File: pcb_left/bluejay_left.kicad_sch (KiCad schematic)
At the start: 72 parts, among them J1 SJ-43514, U1 ATmega328P-PU, Y1 16MHz

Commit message: Further work on pcbs
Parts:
- DZ1, DZ2: footprint Diode_THT_AKL:D_DO-35_SOD27_P7.62mm_Horizontal_Zener -> BlueJay footprints:D_DO-35_SOD27_P5.08mm_Horizontal
- Da1, Da2, Da3, Da4, Da5, Db1, Db2, Db3, Db4, Db5, Dc1, Dc2, Dc3, Dc4, Dc5, Dd1, Dd2, Dd3, Dd4, Dd5, De1, De2, De3, De4, Df2, Df3, Df4: footprint Diode_THT_AKL:D_DO-35_SOD27_P7.62mm_Horizontal -> BlueJay footprints:D_DO-35_SOD27_P5.08mm_Horizontal
- SWa1, SWa2, SWa3, SWa4, SWa5, SWb1, SWb2, SWb3, SWb4, SWb5, SWc1, SWc2, SWc3, SWc4, SWc5, SWd1, SWd2, SWd3, SWd4, SWd5, SWe1, SWe2, SWe3, SWe4, SWf2, SWf3, SWf4: footprint BlueJay footprints:Kailh_socket_MX -> Switch_Keyboard_Cherry_MX:SW_Cherry_MX_PCB_1.00u

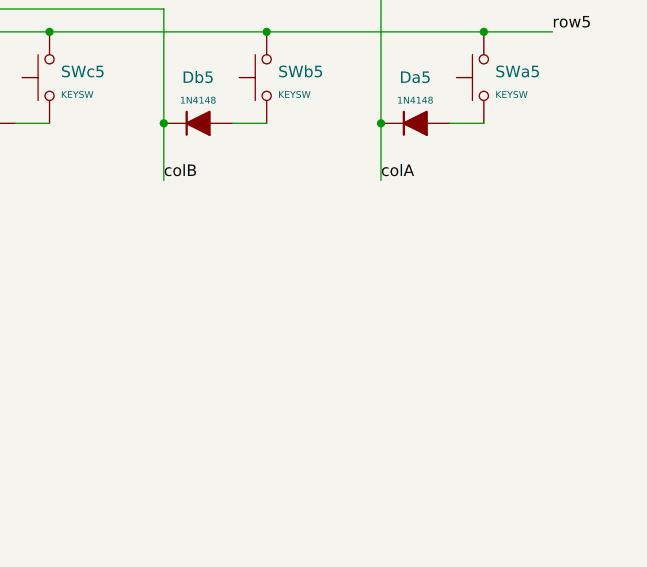
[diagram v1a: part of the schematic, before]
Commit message: Add mounting holes
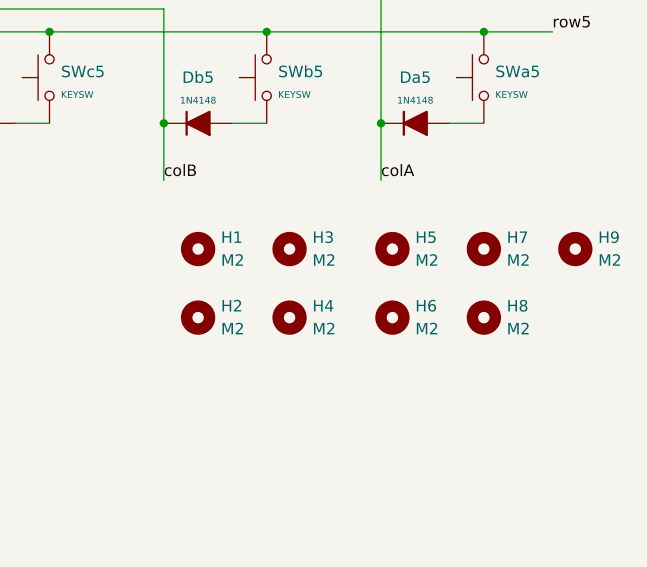
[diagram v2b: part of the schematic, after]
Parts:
- added H1, H2, H3, H4, H5, H6, H7, H8, H9: M2, MountingHole:MountingHole_2.2mm_M2_Pad, symbol Mechanical:MountingHole
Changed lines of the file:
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@@
     (pin "2")
+  )
+  (symbol (lib_id "Mechanical:MountingHole") (at 215.9 162.56 0) (unit 1)
+    (in_bom no) (on_board yes) (fields_autoplaced)
+    (property "Reference" "H2" (id 0) (at 218.44 161.2899 0)
+      (effects (font (size 1.27 1.27)) (justify left))
+    )
+    (property "Value" "M2" (id 1) (at 218.44 163.8299 0)
+      (effects (font (size 1.27 1.27)) (justify left))
+    )
+    (property "Footprint" "MountingHole:MountingHole_2.2mm_M2_Pad" (id 2) (at 215.9 162.56 0)
+      (effects (font (size 1.27 1.27)) hide)
+    )
+    (property "Datasheet" "~" (id 3) (at 215.9 162.56 0)
+      (effects (font (size 1.27 1.27)) hide)
+    )
   )
   (symbol (lib_id "power:GND") (at 93.98 193.04 0) (unit 1)
@@
     (pin "2")
   )
+  (symbol (lib_id "Mechanical:MountingHole") (at 226.06 154.94 0) (unit 1)
+    (in_bom no) (on_board yes) (fields_autoplaced)
+    (property "Reference" "H3" (id 0) (at 228.6 153.6699 0)
+      (effects (font (size 1.27 1.27)) (justify left))
+    )
+    (property "Value" "M2" (id 1) (at 228.6 156.2099 0)
+      (effects (font (size 1.27 1.27)) (justify left))
+    )
+    (property "Footprint" "MountingHole:MountingHole_2.2mm_M2_Pad" (id 2) (at 226.06 154.94 0)
+      (effects (font (size 1.27 1.27)) hide)
+    )
+    (property "Datasheet" "~" (id 3) (at 226.06 154.94 0)
+      (effects (font (size 1.27 1.27)) hide)
+    )
+  )
   (symbol (lib_id "power:PWR_FLAG") (at 29.21 92.71 90) (unit 1)
     (in_bom yes) (on_board yes)
@@
     (pin "1")
     (pin "2")
+  )
+  (symbol (lib_id "Mechanical:MountingHole") (at 237.49 162.56 0) (unit 1)
+    (in_bom no) (on_board yes) (fields_autoplaced)
+    (property "Reference" "H6" (id 0) (at 240.03 161.2899 0)
+      (effects (font (size 1.27 1.27)) (justify left))
+    )
+    (property "Value" "M2" (id 1) (at 240.03 163.8299 0)
+      (effects (font (size 1.27 1.27)) (justify left))
+    )
+    (property "Footprint" "MountingHole:MountingHole_2.2mm_M2_Pad" (id 2) (at 237.49 162.56 0)
+      (effects (font (size 1.27 1.27)) hide)
+    )
+    (property "Datasheet" "~" (id 3) (at 237.49 162.56 0)
+      (effects (font (size 1.27 1.27)) hide)
+    )
   )
   (symbol (lib_id "BlueJaySymbolLibrary:0548190519") (at 24.13 77.47 0) (unit 1)
@@
     (pin "SH")
   )
+  (symbol (lib_id "Mechanical:MountingHole") (at 237.49 154.94 0) (unit 1)
+    (in_bom no) (on_board yes) (fields_autoplaced)
+    (property "Reference" "H5" (id 0) (at 240.03 153.6699 0)
+      (effects (font (size 1.27 1.27)) (justify left))
+    )
+    (property "Value" "M2" (id 1) (at 240.03 156.2099 0)
+      (effects (font (size 1.27 1.27)) (justify left))
+    )
+    (property "Footprint" "MountingHole:MountingHole_2.2mm_M2_Pad" (id 2) (at 237.49 154.94 0)
+      (effects (font (size 1.27 1.27)) hide)
+    )
+    (property "Datasheet" "~" (id 3) (at 237.49 154.94 0)
+      (effects (font (size 1.27 1.27)) hide)
+    )
+  )
   (symbol (lib_id "BlueJaySymbolLibrary:C_Small") (at 59.69 137.16 90) (unit 1)
     (in_bom yes) (on_board yes) (fields_autoplaced)
@@
     (pin "1")
   )
+  (symbol (lib_id "Mechanical:MountingHole") (at 257.81 154.94 0) (unit 1)
+    (in_bom no) (on_board yes) (fields_autoplaced)
+    (property "Reference" "H9" (id 0) (at 260.35 153.6699 0)
+      (effects (font (size 1.27 1.27)) (justify left))
+    )
+    (property "Value" "M2" (id 1) (at 260.35 156.2099 0)
+      (effects (font (size 1.27 1.27)) (justify left))
+    )
+    (property "Footprint" "MountingHole:MountingHole_2.2mm_M2_Pad" (id 2) (at 257.81 154.94 0)
+      (effects (font (size 1.27 1.27)) hide)
+    )
+    (property "Datasheet" "~" (id 3) (at 257.81 154.94 0)
+      (effects (font (size 1.27 1.27)) hide)
+    )
+  )
   (symbol (lib_id "Diode_AKL:1N4148") (at 162.56 99.06 180) (unit 1)
     (in_bom yes) (on_board yes) (fields_autoplaced)
@@
     (pin "1")
     (pin "2")
+  )
+  (symbol (lib_id "Mechanical:MountingHole") (at 247.65 154.94 0) (unit 1)
+    (in_bom no) (on_board yes) (fields_autoplaced)
+    (property "Reference" "H7" (id 0) (at 250.19 153.6699 0)
+      (effects (font (size 1.27 1.27)) (justify left))
+    )
+    (property "Value" "M2" (id 1) (at 250.19 156.2099 0)
+      (effects (font (size 1.27 1.27)) (justify left))
+    )
+    (property "Footprint" "MountingHole:MountingHole_2.2mm_M2_Pad" (id 2) (at 247.65 154.94 0)
+      (effects (font (size 1.27 1.27)) hide)
+    )
+    (property "Datasheet" "~" (id 3) (at 247.65 154.94 0)
+      (effects (font (size 1.27 1.27)) hide)
+    )
   )
   (symbol (lib_id "Diode_AKL:1N4148") (at 138.43 99.06 180) (unit 1)
@@
     (pin "2")
   )
+  (symbol (lib_id "Mechanical:MountingHole") (at 247.65 162.56 0) (unit 1)
+    (in_bom no) (on_board yes) (fields_autoplaced)
+    (property "Reference" "H8" (id 0) (at 250.19 161.2899 0)
+      (effects (font (size 1.27 1.27)) (justify left))
+    )
+    (property "Value" "M2" (id 1) (at 250.19 163.8299 0)
+      (effects (font (size 1.27 1.27)) (justify left))
+    )
+    (property "Footprint" "MountingHole:MountingHole_2.2mm_M2_Pad" (id 2) (at 247.65 162.56 0)
+      (effects (font (size 1.27 1.27)) hide)
+    )
+    (property "Datasheet" "~" (id 3) (at 247.65 162.56 0)
+      (effects (font (size 1.27 1.27)) hide)
+    )
+  )
   (symbol (lib_id "BlueJaySymbolLibrary:Switch_SW_Push") (at 194.31 81.28 90) (unit 1)
     (in_bom yes) (on_board yes) (fields_autoplaced)
@@
     (pin "2")
   )
+  (symbol (lib_id "Mechanical:MountingHole") (at 226.06 162.56 0) (unit 1)
+    (in_bom no) (on_board yes) (fields_autoplaced)
+    (property "Reference" "H4" (id 0) (at 228.6 161.2899 0)
+      (effects (font (size 1.27 1.27)) (justify left))
+    )
+    (property "Value" "M2" (id 1) (at 228.6 163.8299 0)
+      (effects (font (size 1.27 1.27)) (justify left))
+    )
+    (property "Footprint" "MountingHole:MountingHole_2.2mm_M2_Pad" (id 2) (at 226.06 162.56 0)
+      (effects (font (size 1.27 1.27)) hide)
+    )
+    (property "Datasheet" "~" (id 3) (at 226.06 162.56 0)
+      (effects (font (size 1.27 1.27)) hide)
+    )
+  )
   (symbol (lib_id "BlueJaySymbolLibrary:Switch_SW_Push") (at 247.65 135.89 90) (unit 1)
     (in_bom yes) (on_board yes) (fields_autoplaced)
@@
     (pin "1")
     (pin "2")
+  )
+  (symbol (lib_id "Mechanical:MountingHole") (at 215.9 154.94 0) (unit 1)
+    (in_bom no) (on_board yes) (fields_autoplaced)
+    (property "Reference" "H1" (id 0) (at 218.44 153.6699 0)
+      (effects (font (size 1.27 1.27)) (justify left))
+    )
+    (property "Value" "M2" (id 1) (at 218.44 156.2099 0)
+      (effects (font (size 1.27 1.27)) (justify left))
+    )
+    (property "Footprint" "MountingHole:MountingHole_2.2mm_M2_Pad" (id 2) (at 215.9 154.94 0)
+      (effects (font (size 1.27 1.27)) hide)
+    )
+    (property "Datasheet" "~" (id 3) (at 215.9 154.94 0)
+      (effects (font (size 1.27 1.27)) hide)
+    )
   )
   (symbol (lib_id "Diode_AKL:1N4148") (at 90.17 111.76 180) (unit 1)
@@
       (reference "F1") (unit 1) (value "100mA") (footprint "BlueJay footprints:polyfuse_5.1mm")
     )
+    (path "/d0420dde-bff1-4dd4-b50e-a8ff439a9375"
+      (reference "H1") (unit 1) (value "M2") (footprint "MountingHole:MountingHole_2.2mm_M2_Pad")
+    )
+    (path "/4a35a674-388c-438a-8da0-ee33b6fc37e8"
+      (reference "H2") (unit 1) (value "M2") (footprint "MountingHole:MountingHole_2.2mm_M2_Pad")
+    )
+    (path "/552b5d1f-a593-40c3-a973-202071f3c188"
+      (reference "H3") (unit 1) (value "M2") (footprint "MountingHole:MountingHole_2.2mm_M2_Pad")
+    )
+    (path "/c9aec2e8-4e37-4baa-9790-b0363dbc3f18"
+      (reference "H4") (unit 1) (value "M2") (footprint "MountingHole:MountingHole_2.2mm_M2_Pad")
+    )
+    (path "/6dcbd964-e53a-42c2-bb2f-1604534332d7"
+      (reference "H5") (unit 1) (value "M2") (footprint "MountingHole:MountingHole_2.2mm_M2_Pad")
+    )
+    (path "/6133af06-e5a9-4dea-9d88-3fa37672e076"
+      (reference "H6") (unit 1) (value "M2") (footprint "MountingHole:MountingHole_2.2mm_M2_Pad")
+    )
+    (path "/8ff55002-cb98-4e23-b57e-209cc7ec712a"
+      (reference "H7") (unit 1) (value "M2") (footprint "MountingHole:MountingHole_2.2mm_M2_Pad")
+    )
+    (path "/a73aae4f-b04b-4d16-8b11-ca3d57da8772"
+      (reference "H8") (unit 1) (value "M2") (footprint "MountingHole:MountingHole_2.2mm_M2_Pad")
+    )
+    (path "/88babb1f-a86c-44c4-9ecd-f3e8d1f4aef4"
+      (reference "H9") (unit 1) (value "M2") (footprint "MountingHole:MountingHole_2.2mm_M2_Pad")
+    )
     (path "/36a90cbb-ec70-4202-aacd-9cf629bac560"

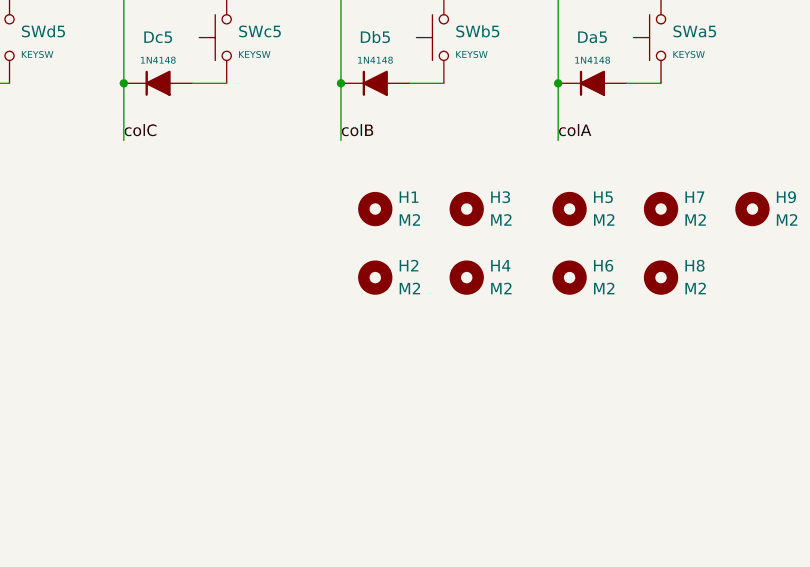
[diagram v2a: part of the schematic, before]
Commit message: Ground a couple mounting holes so as to ground plate and base too
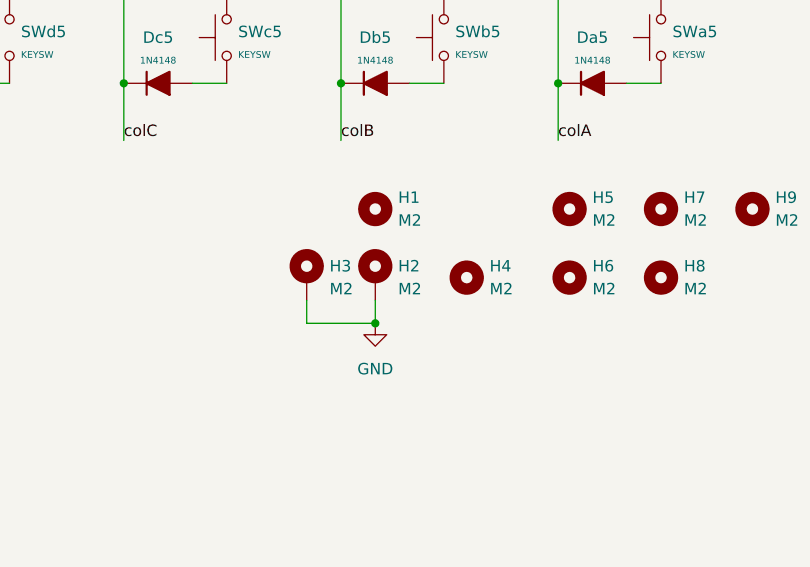
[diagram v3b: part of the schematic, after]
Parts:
- H2, H3: symbol Mechanical:MountingHole -> Mechanical:MountingHole_Pad; now in the parts list
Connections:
- net GND: now also H2.1, H3.1
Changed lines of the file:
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@@
   (junction (at 182.88 111.76) (diameter 0) (color 0 0 0 0)
+  )
+  (junction (at 215.9 167.64) (diameter 0) (color 0 0 0 0)
   )
   (junction (at 207.01 111.76) (diameter 0) (color 0 0 0 0)
@@
     (stroke (width 0) (type default) (color 0 0 0 0))
   )
+  (wire (pts (xy 208.28 167.64) (xy 215.9 167.64))
+    (stroke (width 0) (type default) (color 0 0 0 0))
+  )
   (wire (pts (xy 93.98 184.15) (xy 93.98 185.42))
     (stroke (width 0) (type default) (color 0 0 0 0))
@@
     (stroke (width 0) (type default) (color 0 0 0 0))
   )
+  (wire (pts (xy 208.28 165.1) (xy 208.28 167.64))
+    (stroke (width 0) (type default) (color 0 0 0 0))
+  )
   (wire (pts (xy 118.11 111.76) (xy 121.92 111.76))
     (stroke (width 0) (type default) (color 0 0 0 0))
@@
   )
   (wire (pts (xy 115.57 162.56) (xy 116.84 162.56))
+    (stroke (width 0) (type default) (color 0 0 0 0))
+  )
+  (wire (pts (xy 215.9 165.1) (xy 215.9 167.64))
     (stroke (width 0) (type default) (color 0 0 0 0))
   )
@@
     (pin "2")
   )
-  (symbol (lib_id "Mechanical:MountingHole") (at 215.9 162.56 0) (unit 1)
-    (in_bom no) (on_board yes) (fields_autoplaced)
+  (symbol (lib_id "Mechanical:MountingHole_Pad") (at 215.9 162.56 0) (unit 1)
+    (in_bom yes) (on_board yes) (fields_autoplaced)
     (property "Reference" "H2" (id 0) (at 218.44 161.2899 0)
       (effects (font (size 1.27 1.27)) (justify left))
@@
       (effects (font (size 1.27 1.27)) hide)
     )
+    (pin "1")
   )
   (symbol (lib_id "power:GND") (at 93.98 193.04 0) (unit 1)
@@
     (pin "2")
   )
-  (symbol (lib_id "Mechanical:MountingHole") (at 226.06 154.94 0) (unit 1)
-    (in_bom no) (on_board yes) (fields_autoplaced)
-    (property "Reference" "H3" (id 0) (at 228.6 153.6699 0)
-      (effects (font (size 1.27 1.27)) (justify left))
-    )
-    (property "Value" "M2" (id 1) (at 228.6 156.2099 0)
-      (effects (font (size 1.27 1.27)) (justify left))
-    )
-    (property "Footprint" "MountingHole:MountingHole_2.2mm_M2_Pad" (id 2) (at 226.06 154.94 0)
-      (effects (font (size 1.27 1.27)) hide)
-    )
-    (property "Datasheet" "~" (id 3) (at 226.06 154.94 0)
-      (effects (font (size 1.27 1.27)) hide)
-    )
+  (symbol (lib_id "Mechanical:MountingHole_Pad") (at 208.28 162.56 0) (unit 1)
+    (in_bom yes) (on_board yes) (fields_autoplaced)
+    (property "Reference" "H3" (id 0) (at 210.82 161.2899 0)
+      (effects (font (size 1.27 1.27)) (justify left))
+    )
+    (property "Value" "M2" (id 1) (at 210.82 163.8299 0)
+      (effects (font (size 1.27 1.27)) (justify left))
+    )
+    (property "Footprint" "MountingHole:MountingHole_2.2mm_M2_Pad" (id 2) (at 208.28 162.56 0)
+      (effects (font (size 1.27 1.27)) hide)
+    )
+    (property "Datasheet" "~" (id 3) (at 208.28 162.56 0)
+      (effects (font (size 1.27 1.27)) hide)
+    )
+    (pin "1")
   )
   (symbol (lib_id "power:PWR_FLAG") (at 29.21 92.71 90) (unit 1)
@@
     (pin "1")
     (pin "2")
+  )
+  (symbol (lib_id "power:GND") (at 215.9 167.64 0) (unit 1)
+    (in_bom yes) (on_board yes) (fields_autoplaced)
+    (property "Reference" "#PWR?" (id 0) (at 215.9 173.99 0)
+      (effects (font (size 1.27 1.27)) hide)
+    )
+    (property "Value" "GND" (id 1) (at 215.9 172.72 0))
+    (property "Footprint" "" (id 2) (at 215.9 167.64 0)
+      (effects (font (size 1.27 1.27)) hide)
+    )
+    (property "Datasheet" "" (id 3) (at 215.9 167.64 0)
+      (effects (font (size 1.27 1.27)) hide)
+    )
+    (pin "1")
   )
   (symbol (lib_id "power:VCC") (at 64.77 154.94 0) (unit 1)
@@
       (reference "#PWR0114") (unit 1) (value "GND") (footprint "")
     )
+    (path "/aa799aa4-0b77-4e69-bd3a-b95b04823f1a"
+      (reference "#PWR?") (unit 1) (value "GND") (footprint "")
+    )
     (path "/709a6874-5923-446e-9322-a60e23d13f71"

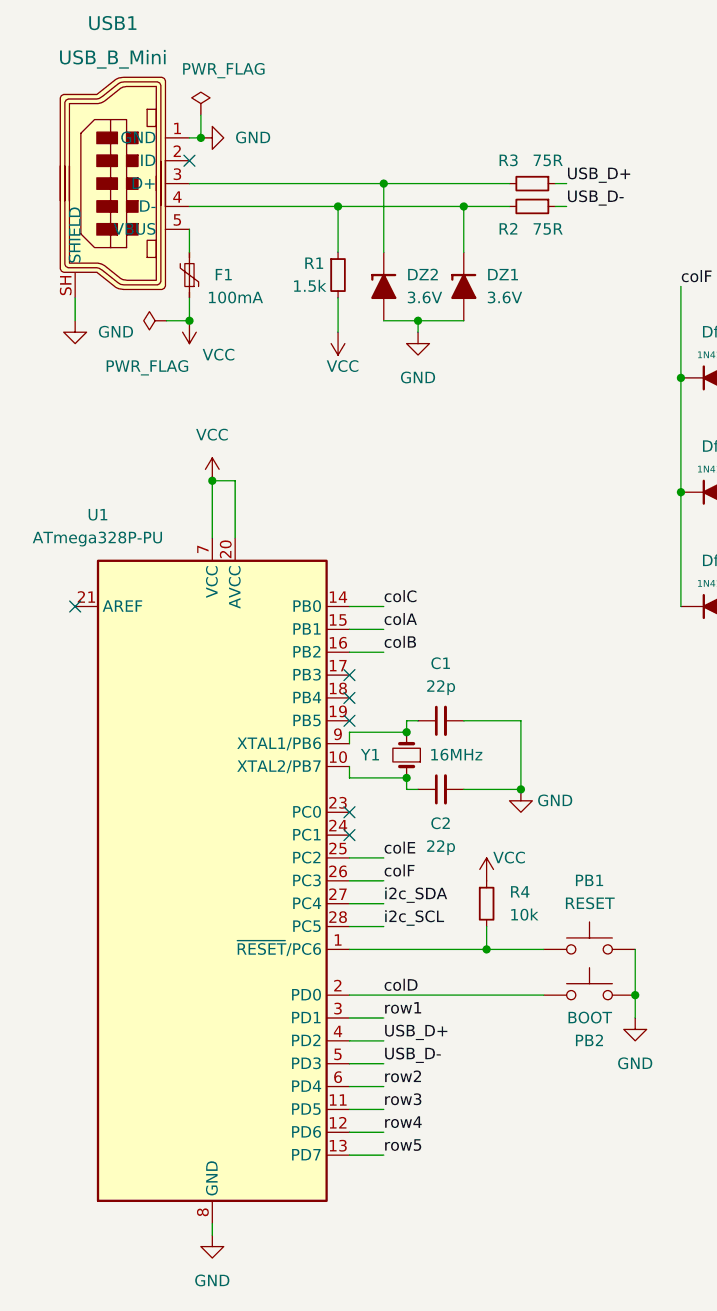
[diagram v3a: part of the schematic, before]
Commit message: Create base pcb
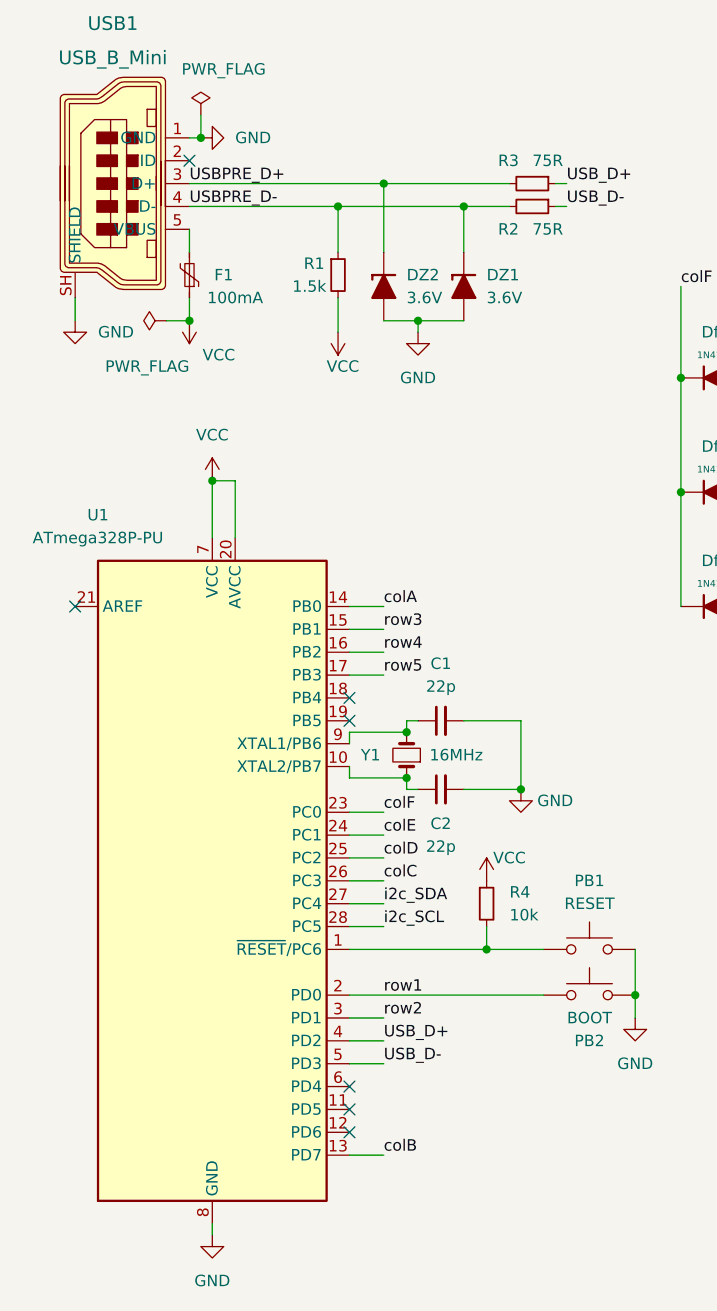
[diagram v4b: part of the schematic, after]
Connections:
- net colA: now also U1.14 (PB0); no longer U1.15 (PB1)
- net colB: now also U1.13 (PD7); no longer U1.16 (PB2)
- net colC: now also U1.26 (PC3); no longer U1.14 (PB0)
- net colD: now also U1.25 (PC2); no longer PB2.1, U1.2 (PD0)
- net colE: now also U1.24 (PC1); no longer U1.25 (PC2)
- net colF: now also U1.23 (PC0); no longer U1.26 (PC3)
- net row1: now also PB2.1, U1.2 (PD0); no longer U1.3 (PD1)
- net row2: now also U1.3 (PD1); no longer U1.6 (PD4)
- net row3: now also U1.15 (PB1); no longer U1.11 (PD5)
- net row4: now also U1.16 (PB2); no longer U1.12 (PD6)
- net row5: now also U1.17 (PB3); no longer U1.13 (PD7)
- net USBPRE_D-: now reaches DZ1.1 (K), R1.1, R2.2, USB1.4 (D-)
- net USBPRE_D+: now reaches DZ2.1 (K), R3.2, USB1.3 (D+)

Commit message: Fine tune pcbs
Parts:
- added J?: Screw_Terminal_01x04, symbol Connector:Screw_Terminal_01x04
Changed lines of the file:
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@@
     (pin "2")
+  )
+  (symbol (lib_id "Connector:Screw_Terminal_01x04") (at 144.78 156.21 90) (unit 1)
+    (in_bom yes) (on_board yes) (fields_autoplaced)
+    (property "Reference" "J?" (id 0) (at 146.05 149.86 90))
+    (property "Value" "Screw_Terminal_01x04" (id 1) (at 146.05 152.4 90))
+    (property "Footprint" "" (id 2) (at 144.78 156.21 0)
+      (effects (font (size 1.27 1.27)) hide)
+    )
+    (property "Datasheet" "~" (id 3) (at 144.78 156.21 0)
+      (effects (font (size 1.27 1.27)) hide)
+    )
+    (pin "1")
+    (pin "2")
+    (pin "3")
+    (pin "4")
   )
   (symbol (lib_id "Diode_AKL:1N4148") (at 138.43 86.36 180) (unit 1)
@@
       (reference "J1") (unit 1) (value "SJ-43514") (footprint "BlueJay footprints:CUI_SJ-43514")
     )
+    (path "/1447b0b5-ab38-407e-b41f-aa727794d4da"
+      (reference "J?") (unit 1) (value "Screw_Terminal_01x04") (footprint "")
+    )
     (path "/31642483-9c10-4ba0-a4b2-91eb418caf17"
